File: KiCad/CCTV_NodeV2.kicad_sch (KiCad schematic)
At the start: 9 parts, among them J1 Solar 6V/10W, J2 Battery (ext, 2× 18650 ||), U1 CN3791, U2 TC4056A_BMS, U3 MT3608, U4 ESP32-S3-DevKitC-1 N16R8, U5 OV7670

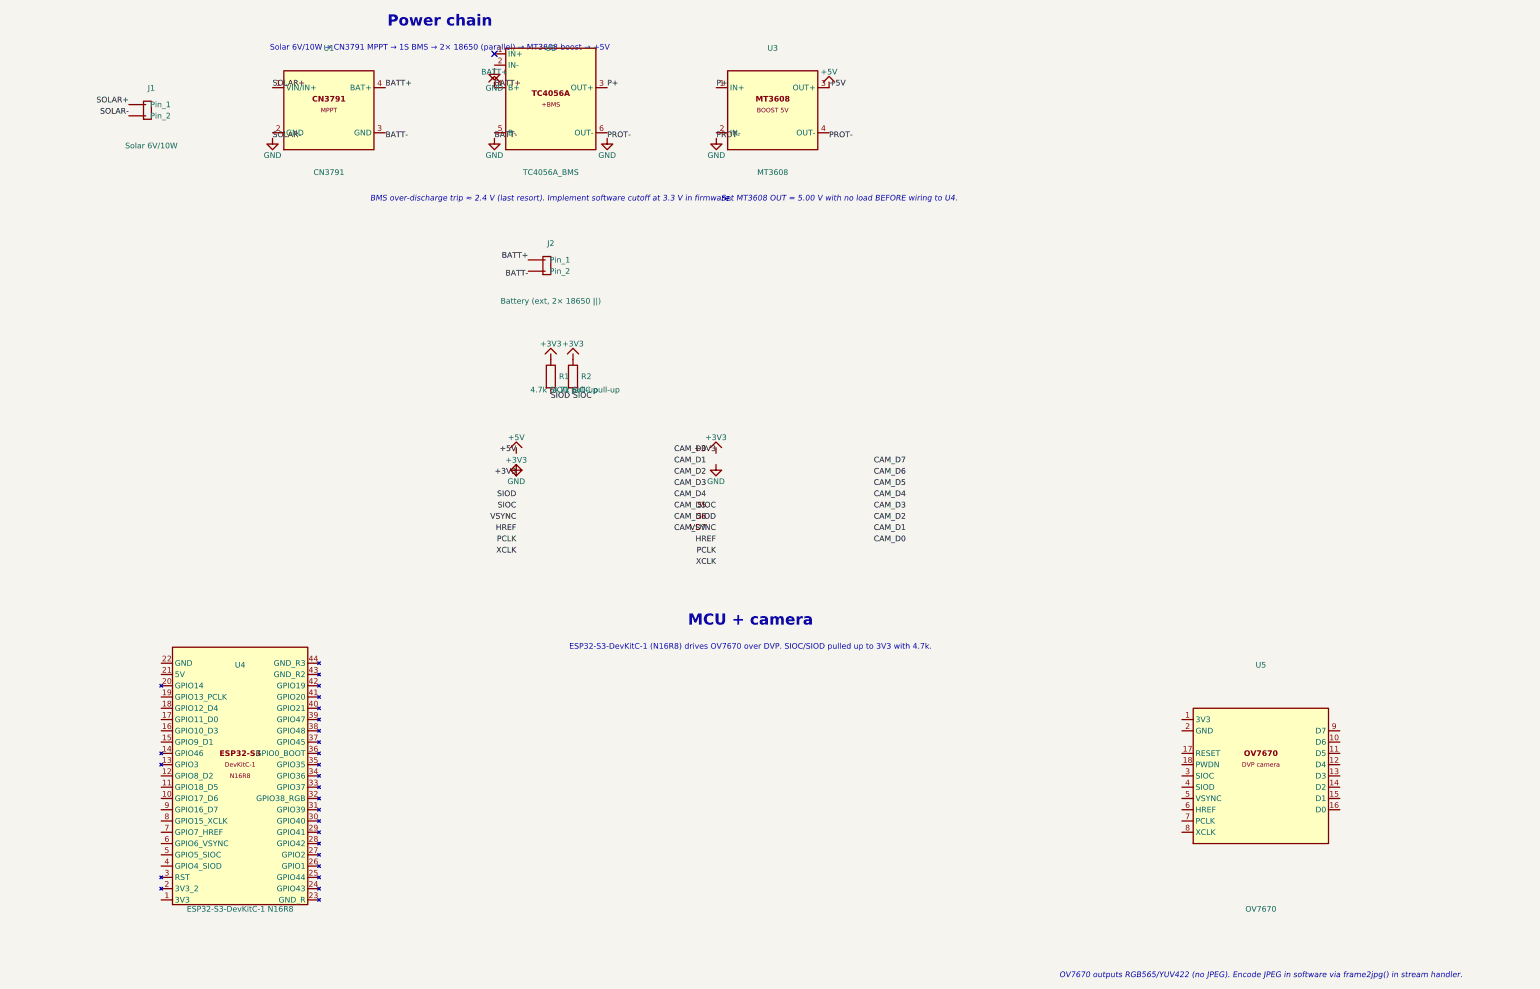
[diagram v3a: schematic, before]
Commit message: Move all wiring labels/power symbols with U4 and U5
All net labels, power symbols (+5V, +3V3, GND) and R1/R2 pull-up
resistors have been relocated to the correct new pin positions.

Because the ESP32-S3 symbol was redesigned with physical pin ordering
(44 pins, new y-coordinates per pin), labels could NOT simply shift
by a fixed offset — each needed its own target y calculated as:
  new_y = placed_y(220) − symbol_pin_y

U4 (60, 220) — left column labels now at x=42.22:
  +5V   → (42.22, 197.14)  [pin 21]
  GND   → (42.22, 194.60)  [pin 22]
  +3V3  → (42.22, 247.94)  [pin 1]
  SIOD  → (42.22, 240.32)  [pin 4 GPIO4]
  SIOC  → (42.22, 237.78)  [pin 5 GPIO5]
  VSYNC → (42.22, 235.24)  [pin 6 GPIO6]
  HREF  → (42.22, 232.70)  [pin 7 GPIO7]
  XCLK  → (42.22, 230.16)  [pin 8 GPIO15]
  CAM_D7→ (42.22, 227.62)  [pin 9 GPIO16]
  CAM_D6→ (42.22, 225.08)  [pin 10 GPIO17]
  CAM_D5→ (42.22, 222.54)  [pin 11 GPIO18]
  CAM_D2→ (42.22, 220.00)  [pin 12 GPIO8]
  CAM_D1→ (42.22, 212.38)  [pin 15 GPIO9]
  CAM_D3→ (42.22, 209.84)  [pin 16 GPIO10]
  CAM_D0→ (42.22, 207.30)  [pin 17 GPIO11]
  CAM_D4→ (42.22, 204.76)  [pin 18 GPIO12]
  PCLK  → (42.22, 202.22)  [pin 19 GPIO13]

U5 (290, 220) — left column at x=272.22, right at x=307.78:
  +3V3/GND/SIOC/SIOD/VSYNC/HREF/PCLK/XCLK on left
  CAM_D0-D7 on right column

R1/R2 SIOD/SIOC pull-ups: (130/135, 130) → (50/55, 232)
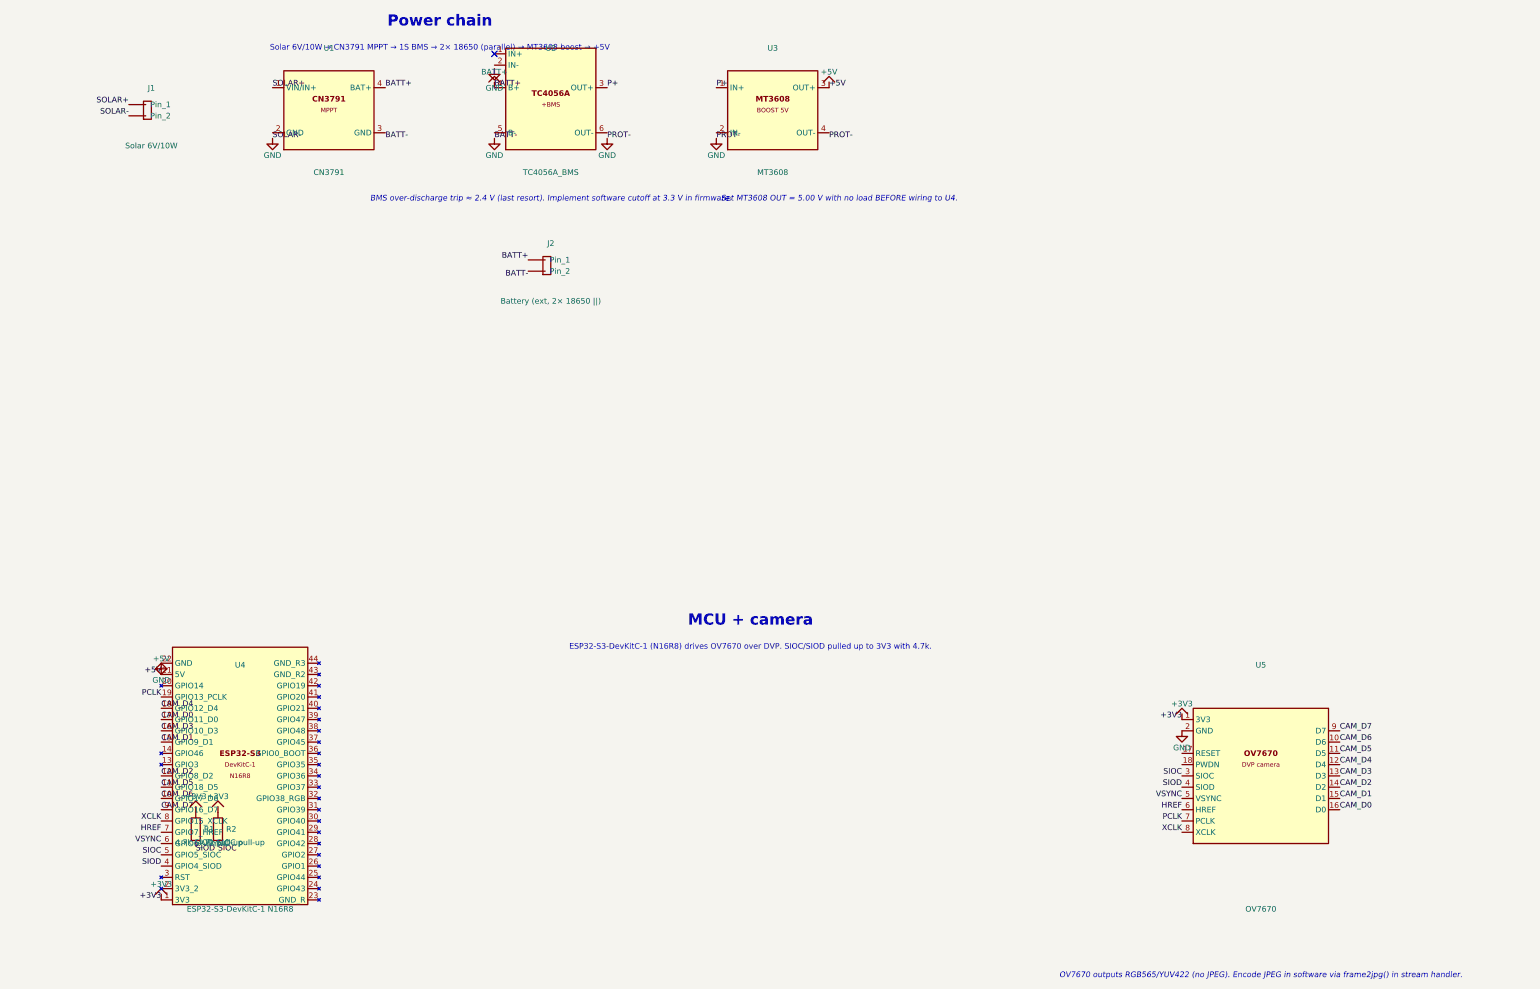
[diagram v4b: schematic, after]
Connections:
- net +3V3: now also U4.1 (3V3), U5.1 (3V3)
- net +5V: now also U4.21 (5V)
- net CAM_D0: now also U4.17 (GPIO11_D0), U5.16 (D0)
- net CAM_D1: now also U4.15 (GPIO9_D1), U5.15 (D1)
- net CAM_D2: now also U4.12 (GPIO8_D2), U5.14 (D2)
- net CAM_D3: now also U4.16 (GPIO10_D3), U5.13 (D3)
- net CAM_D4: now also U4.18 (GPIO12_D4), U5.12 (D4)
- net CAM_D5: now also U4.11 (GPIO18_D5), U5.11 (D5)
- net CAM_D6: now also U4.10 (GPIO17_D6), U5.10 (D6)
- net CAM_D7: now also U4.9 (GPIO16_D7), U5.9 (D7)
- net GND: now also U4.22 (GND), U5.2 (GND)
- net HREF: now also U4.7 (GPIO7_HREF), U5.6 (HREF)
- net PCLK: now also U4.19 (GPIO13_PCLK), U5.7 (PCLK)
- net SIOC: now also U4.5 (GPIO5_SIOC), U5.3 (SIOC)
- net SIOD: now also U4.4 (GPIO4_SIOD), U5.4 (SIOD)
- net VSYNC: now also U4.6 (GPIO6_VSYNC), U5.5 (VSYNC)
- net XCLK: now also U4.8 (GPIO15_XCLK), U5.8 (XCLK)
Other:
- moved on the sheet: R1, R2
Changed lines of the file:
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@@
 	(symbol
 		(lib_id "CCTV2:R")
-		(at 130 130 0)
+		(at 50 232 0)
 		(unit 1)
 		(in_bom yes)
@@
 		(dnp no)
 		(property "Reference" "R1"
-			(at 133 130 0)
+			(at 53 232 0)
 		)
 		(property "Value" "4.7k SIOD pull-up"
-			(at 133 133 0)
+			(at 53 235 0)
 		)
 		(property "Footprint" "Resistor_THT:R_Axial_DIN0207_L6.3mm_D2.5mm_P7.62mm_Horizontal"
@@
 	(symbol
 		(lib_id "CCTV2:R")
-		(at 135 130 0)
+		(at 55 232 0)
 		(unit 1)
 		(in_bom yes)
@@
 		(dnp no)
 		(property "Reference" "R2"
-			(at 138 130 0)
+			(at 58 232 0)
 		)
 		(property "Value" "4.7k SIOC pull-up"
-			(at 138 133 0)
+			(at 58 235 0)
 		)
 		(property "Footprint" "Resistor_THT:R_Axial_DIN0207_L6.3mm_D2.5mm_P7.62mm_Horizontal"
@@
 	(symbol
 		(lib_id "CCTV2:+5V")
-		(at 122.22 147.3 0)
+		(at 42.22 197.14 0)
 		(unit 1)
 		(in_bom yes)
@@
 		(dnp no)
 		(property "Reference" "#PWR02"
-			(at 122.22 143.49 0)
+			(at 42.22 193.33 0)
 			(hide yes)
 		)
 		(property "Value" "+5V"
-			(at 122.22 143.74 0)
+			(at 42.22 193.58 0)
 		)
 		(pin "1")
@@
 	(symbol
 		(lib_id "CCTV2:+3V3")
-		(at 122.22 152.38 0)
+		(at 42.22 247.94 0)
 		(unit 1)
 		(in_bom yes)
@@
 		(dnp no)
 		(property "Reference" "#PWR03"
-			(at 122.22 148.57 0)
+			(at 42.22 244.13 0)
 			(hide yes)
 		)
 		(property "Value" "+3V3"
-			(at 122.22 148.82 0)
+			(at 42.22 244.38 0)
 		)
 		(pin "1")
@@
 	(symbol
 		(lib_id "CCTV2:+3V3")
-		(at 167.22 147.3 0)
+		(at 272.22 207.30 0)
 		(unit 1)
 		(in_bom yes)
@@
 		(dnp no)
 		(property "Reference" "#PWR04"
-			(at 167.22 143.49 0)
+			(at 272.22 203.49 0)
 			(hide yes)
 		)
 		(property "Value" "+3V3"
-			(at 167.22 143.74 0)
+			(at 272.22 203.74 0)
 		)
 		(pin "1")
@@
 	(symbol
 		(lib_id "CCTV2:+3V3")
-		(at 130 126.19 0)
+		(at 50 228.19 0)
 		(unit 1)
 		(in_bom yes)
@@
 		(dnp no)
 		(property "Reference" "#PWR05"
-			(at 130 122.38 0)
+			(at 50 224.38 0)
 			(hide yes)
 		)
 		(property "Value" "+3V3"
-			(at 130 122.63 0)
+			(at 50 224.63 0)
 		)
 		(pin "1")
@@
 	(symbol
 		(lib_id "CCTV2:+3V3")
-		(at 135 126.19 0)
+		(at 55 228.19 0)
 		(unit 1)
 		(in_bom yes)
@@
 		(dnp no)
 		(property "Reference" "#PWR06"
-			(at 135 122.38 0)
+			(at 55 224.38 0)
 			(hide yes)
 		)
 		(property "Value" "+3V3"
-			(at 135 122.63 0)
+			(at 55 224.63 0)
 		)
 		(pin "1")
@@
 	(symbol
 		(lib_id "CCTV2:GND")
-		(at 122.22 149.84 0)
+		(at 42.22 194.60 0)
 		(unit 1)
 		(in_bom yes)
@@
 		(dnp no)
 		(property "Reference" "#PWR14"
-			(at 122.22 156.19 0)
-			(hide yes)
-		)
-		(property "Value" "GND"
-			(at 122.22 153.65 0)
+			(at 42.22 200.95 0)
+			(hide yes)
+		)
+		(property "Value" "GND"
+			(at 42.22 198.41 0)
 		)
 		(pin "1")
@@
 	(symbol
 		(lib_id "CCTV2:GND")
-		(at 167.22 149.84 0)
+		(at 272.22 209.84 0)
 		(unit 1)
 		(in_bom yes)
@@
 		(dnp no)
 		(property "Reference" "#PWR15"
-			(at 167.22 156.19 0)
-			(hide yes)
-		)
-		(property "Value" "GND"
-			(at 167.22 153.65 0)
+			(at 272.22 216.19 0)
+			(hide yes)
+		)
+		(property "Value" "GND"
+			(at 272.22 213.65 0)
 		)
 		(pin "1")
@@
 	)
 	(label "+5V"
-		(at 122.22 147.3 0)
+		(at 42.22 197.14 0)
 		(effects (font (size 1.27 1.27)) (justify right bottom))
 	)
 	(label "+3V3"
-		(at 122.22 152.38 0)
+		(at 42.22 247.94 0)
 		(effects (font (size 1.27 1.27)) (justify right bottom))
 	)
 	(label "SIOD"
-		(at 122.22 157.46 0)
+		(at 42.22 240.32 0)
 		(effects (font (size 1.27 1.27)) (justify right bottom))
 	)
 	(label "SIOC"
-		(at 122.22 160 0)
+		(at 42.22 237.78 0)
 		(effects (font (size 1.27 1.27)) (justify right bottom))
 	)
 	(label "VSYNC"
-		(at 122.22 162.54 0)
+		(at 42.22 235.24 0)
 		(effects (font (size 1.27 1.27)) (justify right bottom))
 	)
 	(label "HREF"
-		(at 122.22 165.08 0)
+		(at 42.22 232.70 0)
 		(effects (font (size 1.27 1.27)) (justify right bottom))
 	)
 	(label "PCLK"
-		(at 122.22 167.62 0)
+		(at 42.22 202.22 0)
 		(effects (font (size 1.27 1.27)) (justify right bottom))
 	)
 	(label "XCLK"
-		(at 122.22 170.16 0)
+		(at 42.22 230.16 0)
 		(effects (font (size 1.27 1.27)) (justify right bottom))
 	)
 	(label "CAM_D0"
-		(at 157.78 147.3 0)
+		(at 42.22 207.30 0)
 		(effects (font (size 1.27 1.27)) (justify left bottom))
 	)
 	(label "CAM_D1"
-		(at 157.78 149.84 0)
+		(at 42.22 212.38 0)
 		(effects (font (size 1.27 1.27)) (justify left bottom))
 	)
 	(label "CAM_D2"
-		(at 157.78 152.38 0)
+		(at 42.22 220.00 0)
 		(effects (font (size 1.27 1.27)) (justify left bottom))
 	)
 	(label "CAM_D3"
-		(at 157.78 154.92 0)
+		(at 42.22 209.84 0)
 		(effects (font (size 1.27 1.27)) (justify left bottom))
 	)
 	(label "CAM_D4"
-		(at 157.78 157.46 0)
+		(at 42.22 204.76 0)
 		(effects (font (size 1.27 1.27)) (justify left bottom))
 	)
 	(label "CAM_D5"
-		(at 157.78 160 0)
+		(at 42.22 222.54 0)
 		(effects (font (size 1.27 1.27)) (justify left bottom))
 	)
 	(label "CAM_D6"
-		(at 157.78 162.54 0)
+		(at 42.22 225.08 0)
 		(effects (font (size 1.27 1.27)) (justify left bottom))
 	)
 	(label "CAM_D7"
-		(at 157.78 165.08 0)
+		(at 42.22 227.62 0)
 		(effects (font (size 1.27 1.27)) (justify left bottom))
 	)
 	(label "+3V3"
-		(at 167.22 147.3 0)
+		(at 272.22 207.30 0)
 		(effects (font (size 1.27 1.27)) (justify right bottom))
 	)
 	(label "SIOC"
-		(at 167.22 160 0)
+		(at 272.22 220.00 0)
 		(effects (font (size 1.27 1.27)) (justify right bottom))
 	)
 	(label "SIOD"
-		(at 167.22 162.54 0)
+		(at 272.22 222.54 0)
 		(effects (font (size 1.27 1.27)) (justify right bottom))
 	)
 	(label "VSYNC"
-		(at 167.22 165.08 0)
+		(at 272.22 225.08 0)
 		(effects (font (size 1.27 1.27)) (justify right bottom))
 	)
 	(label "HREF"
-		(at 167.22 167.62 0)
+		(at 272.22 227.62 0)
 		(effects (font (size 1.27 1.27)) (justify right bottom))
 	)
 	(label "PCLK"
-		(at 167.22 170.16 0)
+		(at 272.22 230.16 0)
 		(effects (font (size 1.27 1.27)) (justify right bottom))
 	)
 	(label "XCLK"
-		(at 167.22 172.7 0)
+		(at 272.22 232.70 0)
 		(effects (font (size 1.27 1.27)) (justify right bottom))
 	)
 	(label "CAM_D7"
-		(at 202.78 149.84 0)
+		(at 307.78 209.84 0)
 		(effects (font (size 1.27 1.27)) (justify left bottom))
 	)
 	(label "CAM_D6"
-		(at 202.78 152.38 0)
+		(at 307.78 212.38 0)
 		(effects (font (size 1.27 1.27)) (justify left bottom))
 	)
 	(label "CAM_D5"
-		(at 202.78 154.92 0)
+		(at 307.78 214.92 0)
 		(effects (font (size 1.27 1.27)) (justify left bottom))
 	)
 	(label "CAM_D4"
-		(at 202.78 157.46 0)
+		(at 307.78 217.46 0)
 		(effects (font (size 1.27 1.27)) (justify left bottom))
 	)
 	(label "CAM_D3"
-		(at 202.78 160 0)
+		(at 307.78 220.00 0)
 		(effects (font (size 1.27 1.27)) (justify left bottom))
 	)
 	(label "CAM_D2"
-		(at 202.78 162.54 0)
+		(at 307.78 222.54 0)
 		(effects (font (size 1.27 1.27)) (justify left bottom))
 	)
 	(label "CAM_D1"
-		(at 202.78 165.08 0)
+		(at 307.78 225.08 0)
 		(effects (font (size 1.27 1.27)) (justify left bottom))
 	)
 	(label "CAM_D0"
-		(at 202.78 167.62 0)
+		(at 307.78 227.62 0)
 		(effects (font (size 1.27 1.27)) (justify left bottom))
 	)
 	(label "SIOD"
-		(at 130 133.81 0)
+		(at 50 235.81 0)
 		(effects (font (size 1.27 1.27)) (justify left top))
 	)
 	(label "SIOC"
-		(at 135 133.81 0)
-		(effects (font (size 1.27 1.27)) (justify left top))
-	)
+		(at 55 235.81 0)
+		(effects (font (size 1.27 1.27)) (justify left top))
+	)
